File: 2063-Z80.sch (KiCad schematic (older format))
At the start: 80 parts, among them J1 Conn_01x05, J10 Conn_01x07, J11 Conn_02x03_Odd_Even, J2 DM3D-SF(41), J3 Conn_02x20_Counter_Clockwise, J4 Conn_02x05_Odd_Even, J5 Conn_02x05_Odd_Even, J6 0548190519, J7 Conn_02x13_Top_Bottom, J8 Conn_01x05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

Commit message: Clean up BOM values & formatting
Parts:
- J11: value Conn_02x03_Odd_Even -> Conn_02x03
- J3: value Conn_02x20_Counter_Clockwise -> Conn_02x20
- J4, J5: value Conn_02x05_Odd_Even -> Conn_02x05
- J7: value Conn_02x13_Top_Bottom -> Conn_02x13
- LOGO1, LOGO2: value Logo_Open_Hardware_Small -> OSHW_Logo
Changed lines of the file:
@@
 P 15550 5900
 F 0 "J3" H 15600 6950 50  0000 C CNN
-F 1 "Conn_02x20_Counter_Clockwise" H 15600 6926 50  0001 C CNN
+F 1 "Conn_02x20" H 15600 6926 50  0001 C CNN
 F 2 "jb-footprint:PinHeader_2x20_P2.54mm_Vertical_counterclock" H 15550 5900 50  0001 C CNN
 F 3 "https://drawings-pdf.s3.amazonaws.com/11636.pdf" H 15550 5900 50  0001 C CNN
@@
 P 15550 3650
 F 0 "J7" H 15600 4400 50  0000 C CNN
-F 1 "Conn_02x13_Top_Bottom" H 15600 4376 50  0001 C CNN
+F 1 "Conn_02x13" H 15600 4376 50  0001 C CNN
 F 2 "jb-footprint:PinHeader_2x13_P2.54mm_Top_Bottom" H 15550 3650 50  0001 C CNN
 F 3 "https://drawings-pdf.s3.amazonaws.com/11636.pdf" H 15550 3650 50  0001 C CNN
@@
 AR Path="/611D78B5" Ref="LOGO1"  Part="1"
 F 0 "LOGO1" H 16250 9875 50  0001 C CNN
-F 1 "Logo_Open_Hardware_Small" H 16250 9375 50  0001 C CNN
+F 1 "OSHW_Logo" H 16250 9375 50  0001 C CNN
 F 2 "Symbol:OSHW-Logo_11.4x12mm_SilkScreen" H 16250 9600 50  0001 C CNN
 F 3 "" H 16250 9600 50  0001 C CNN
@@
 AR Path="/61291DA5" Ref="LOGO2"  Part="1"
 F 0 "LOGO2" H 16200 8125 50  0001 C CNN
-F 1 "Logo_Open_Hardware_Small" H 16200 7625 50  0001 C CNN
+F 1 "OSHW_Logo" H 16200 7625 50  0001 C CNN
 F 2 "Symbol:OSHW-Logo_5.7x6mm_SilkScreen" H 16200 7850 50  0001 C CNN
 F 3 "" H 16200 7850 50  0001 C CNN
@@
 P 11600 8450
 F 0 "J4" H 11650 8775 50  0000 C CNN
-F 1 "Conn_02x05_Odd_Even" H 11650 8776 50  0001 C CNN
+F 1 "Conn_02x05" H 11650 8776 50  0001 C CNN
 F 2 "Connector_PinHeader_2.54mm:PinHeader_2x05_P2.54mm_Vertical" H 11600 8450 50  0001 C CNN
 F 3 "" H 11600 8450 50  0001 C CNN
@@
 P 11650 9650
 F 0 "J5" H 11700 9975 50  0000 C CNN
-F 1 "Conn_02x05_Odd_Even" H 11700 9976 50  0001 C CNN
+F 1 "Conn_02x05" H 11700 9976 50  0001 C CNN
 F 2 "Connector_PinHeader_2.54mm:PinHeader_2x05_P2.54mm_Vertical" H 11650 9650 50  0001 C CNN
 F 3 "" H 11650 9650 50  0001 C CNN
@@
 P 11800 3150
 F 0 "J11" H 11850 3350 50  0000 C CNN
-F 1 "Conn_02x03_Odd_Even" H 11850 3376 50  0001 C CNN
+F 1 "Conn_02x03" H 11850 3376 50  0001 C CNN
 F 2 "Connector_PinHeader_2.54mm:PinHeader_2x03_P2.54mm_Vertical" H 11800 3150 50  0001 C CNN
 F 3 "https://app.adam-tech.com/products/download/data_sheet/202065/ph2-xx-ua-data-sheet.pdf" H 11800 3150 50  0001 C CNN

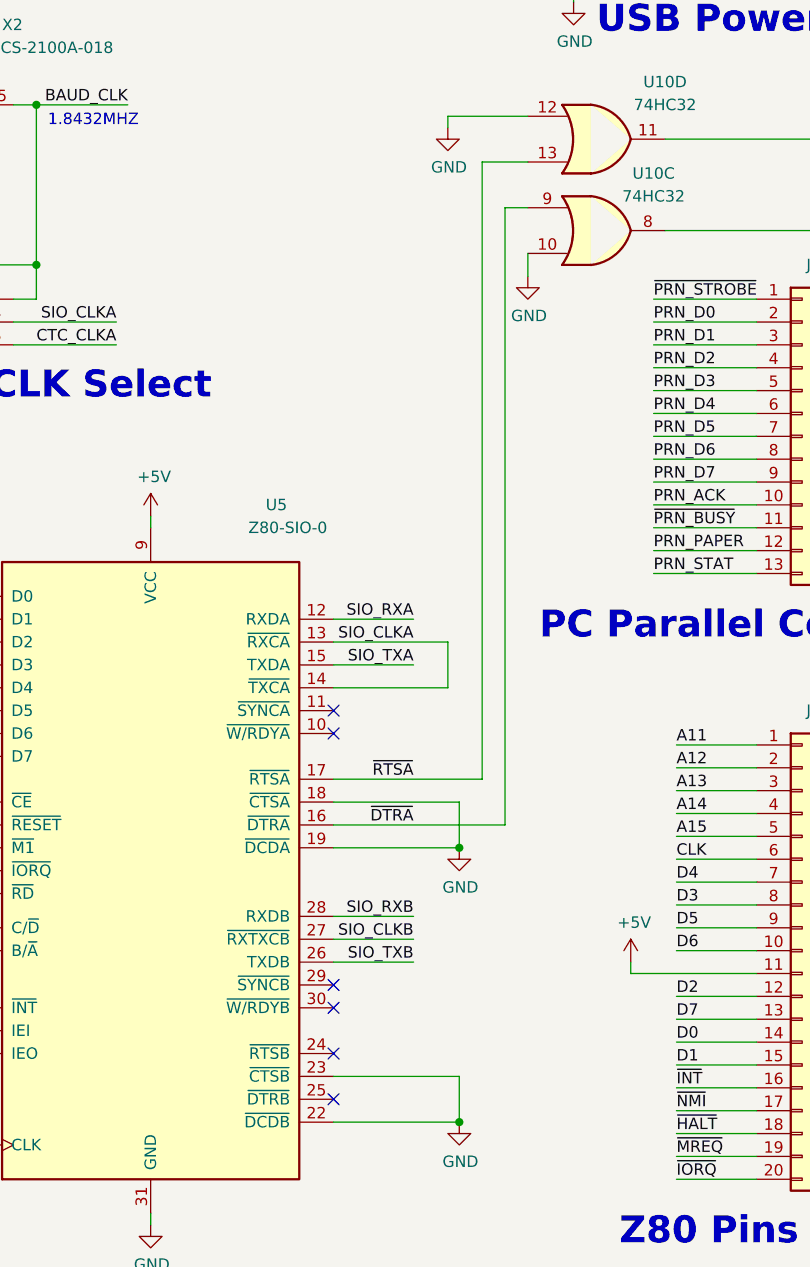
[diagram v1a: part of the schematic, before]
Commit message: Move ~PRN_LF from U5.17 to U5.25
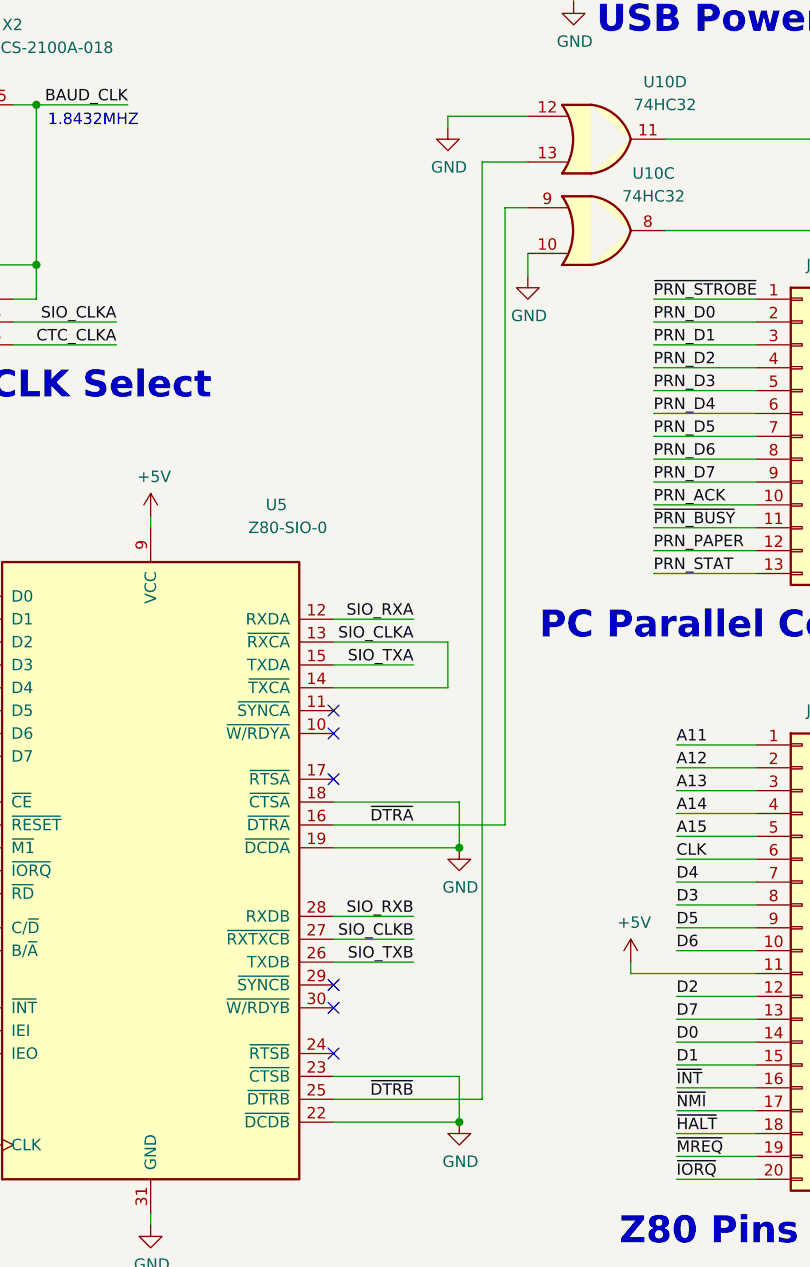
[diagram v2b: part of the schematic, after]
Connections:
- net ~DTRB: now reaches U5.25 (~DTRB)
- net ~DTRB: now also U10.13
- net ~RTSA: no longer names the net of U5.17 (~RTSA)
- net ~RTSA: no longer U10.13
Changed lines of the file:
@@
 Sheet 1 1
 Title "Z80 Retro Board"
-Date "2021-10-13"
-Rev "3"
+Date "2021-12-01"
+Rev "4"
 Comp ""
 Comment1 ""
@@
 	13500 6650 14050 6650
 NoConn ~ 13500 6350
-NoConn ~ 13500 6550
 Text Label 750  1600 0    50   ~ 0
 ~IORQ_70
@@
 Text Label 2750 4200 0    50   ~ 0
 BA15
-Text Label 13850 5150 2    50   ~ 0
-~RTSA
 Wire Wire Line
-	14150 2450 14150 5150
+	14150 2450 14150 6550
 $Comp
 L power:GND #PWR0156
@@
 Wire Wire Line
 	7250 700  7250 750
-Wire Wire Line
-	13500 5150 14150 5150
 Connection ~ 4900 1450
 Connection ~ 4900 1650
@@
 	1    0    0    -1
 $EndComp
+NoConn ~ 13500 5150
+Wire Wire Line
+	13500 6550 14150 6550
+Text Label 13850 6550 2    50   ~ 0
+~DTRB
 $EndSCHEMATC

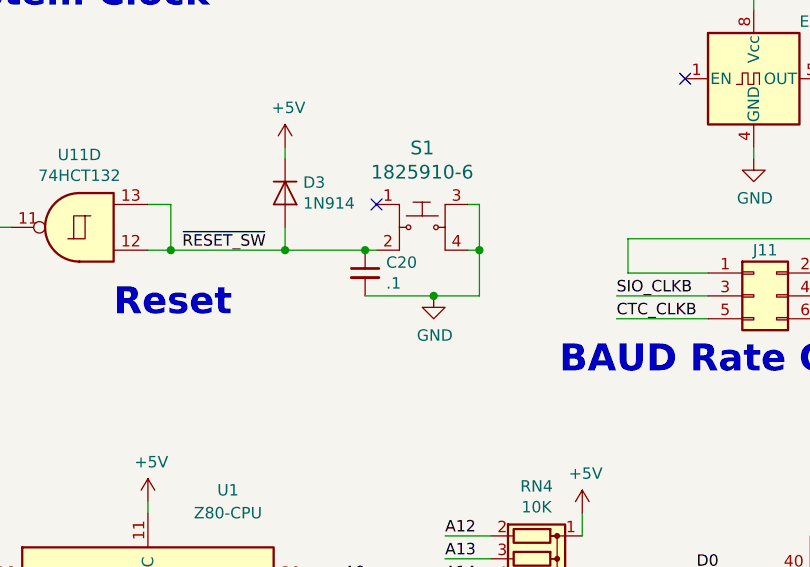
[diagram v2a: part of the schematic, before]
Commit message: Change C20 to .47uF to make RESET last 4X longer
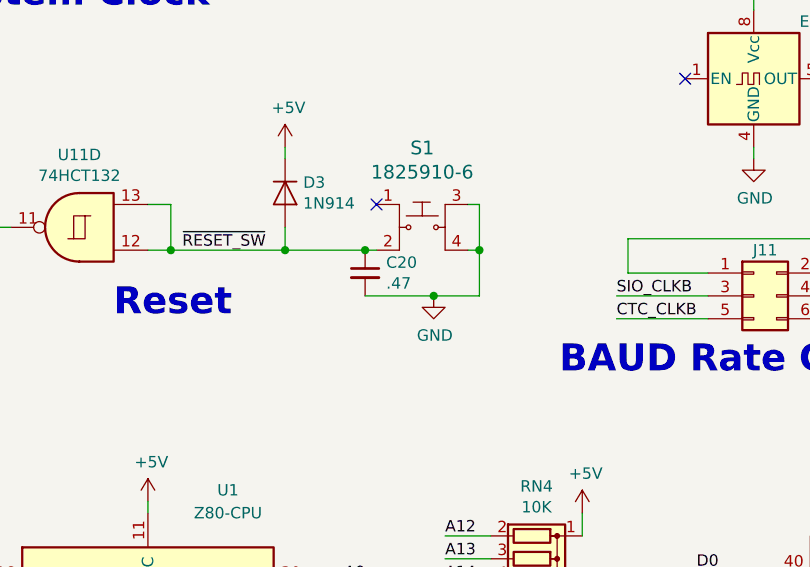
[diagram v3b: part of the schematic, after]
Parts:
- C1, C10, C11, C12, C13, C14, C15, C16, C2, C21, C22, C23, C3, C4, C5, C6, C7, C8, C9: Digi-Key_PN 399-9859-1-ND‎ -> 399-9859-1-ND
- C20: value .1 -> .47; Description CAP CER 0.1UF 50V Z5U RADIAL -> CAP CER 0.47UF 50V X7R RADIAL; Digi-Key_PN 399-9859-1-ND‎ -> 399-14039-1-ND; MPN ‎C315C104M5U5TA7303‎ -> C315C474K5R5TA7303
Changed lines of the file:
@@
 F 2 "Capacitor_THT:C_Disc_D3.0mm_W2.0mm_P2.50mm" H 4000 950 50  0001 C CNN
 F 3 "https://api.kemet.com/component-edge/download/specsheet/C315C104M5U5TA7303.pdf" H 4000 950 50  0001 C CNN
-F 4 "399-9859-1-ND‎" H 4000 950 50  0001 C CNN "Digi-Key_PN"
+F 4 "399-9859-1-ND" H 4000 950 50  0001 C CNN "Digi-Key_PN"
 F 5 "‎C315C104M5U5TA7303‎" H 4000 950 50  0001 C CNN "MPN"
 F 6 "CAP CER 0.1UF 50V Z5U RADIAL" H 4000 950 50  0001 C CNN "Description"
@@
 F 2 "Capacitor_THT:C_Disc_D3.0mm_W2.0mm_P2.50mm" H 4300 950 50  0001 C CNN
 F 3 "https://api.kemet.com/component-edge/download/specsheet/C315C104M5U5TA7303.pdf" H 4300 950 50  0001 C CNN
-F 4 "399-9859-1-ND‎" H 4300 950 50  0001 C CNN "Digi-Key_PN"
+F 4 "399-9859-1-ND" H 4300 950 50  0001 C CNN "Digi-Key_PN"
 F 5 "‎C315C104M5U5TA7303‎" H 4300 950 50  0001 C CNN "MPN"
 F 6 "CAP CER 0.1UF 50V Z5U RADIAL" H 4300 950 50  0001 C CNN "Description"
@@
 F 2 "Capacitor_THT:C_Disc_D3.0mm_W2.0mm_P2.50mm" H 4600 950 50  0001 C CNN
 F 3 "https://api.kemet.com/component-edge/download/specsheet/C315C104M5U5TA7303.pdf" H 4600 950 50  0001 C CNN
-F 4 "399-9859-1-ND‎" H 4600 950 50  0001 C CNN "Digi-Key_PN"
+F 4 "399-9859-1-ND" H 4600 950 50  0001 C CNN "Digi-Key_PN"
 F 5 "‎C315C104M5U5TA7303‎" H 4600 950 50  0001 C CNN "MPN"
 F 6 "CAP CER 0.1UF 50V Z5U RADIAL" H 4600 950 50  0001 C CNN "Description"
@@
 F 2 "Capacitor_THT:C_Disc_D3.0mm_W2.0mm_P2.50mm" H 4900 950 50  0001 C CNN
 F 3 "https://api.kemet.com/component-edge/download/specsheet/C315C104M5U5TA7303.pdf" H 4900 950 50  0001 C CNN
-F 4 "399-9859-1-ND‎" H 4900 950 50  0001 C CNN "Digi-Key_PN"
+F 4 "399-9859-1-ND" H 4900 950 50  0001 C CNN "Digi-Key_PN"
 F 5 "‎C315C104M5U5TA7303‎" H 4900 950 50  0001 C CNN "MPN"
 F 6 "CAP CER 0.1UF 50V Z5U RADIAL" H 4900 950 50  0001 C CNN "Description"
@@
 F 2 "Capacitor_THT:C_Disc_D3.0mm_W2.0mm_P2.50mm" H 5200 950 50  0001 C CNN
 F 3 "https://api.kemet.com/component-edge/download/specsheet/C315C104M5U5TA7303.pdf" H 5200 950 50  0001 C CNN
-F 4 "399-9859-1-ND‎" H 5200 950 50  0001 C CNN "Digi-Key_PN"
+F 4 "399-9859-1-ND" H 5200 950 50  0001 C CNN "Digi-Key_PN"
 F 5 "‎C315C104M5U5TA7303‎" H 5200 950 50  0001 C CNN "MPN"
 F 6 "CAP CER 0.1UF 50V Z5U RADIAL" H 5200 950 50  0001 C CNN "Description"
@@
 F 2 "Capacitor_THT:C_Disc_D3.0mm_W2.0mm_P2.50mm" H 7000 8400 50  0001 C CNN
 F 3 "https://api.kemet.com/component-edge/download/specsheet/C315C104M5U5TA7303.pdf" H 7000 8400 50  0001 C CNN
-F 4 "399-9859-1-ND‎" H 7000 8400 50  0001 C CNN "Digi-Key_PN"
+F 4 "399-9859-1-ND" H 7000 8400 50  0001 C CNN "Digi-Key_PN"
 F 5 "‎C315C104M5U5TA7303‎" H 7000 8400 50  0001 C CNN "MPN"
 F 6 "CAP CER 0.1UF 50V Z5U RADIAL" H 7000 8400 50  0001 C CNN "Description"
@@
 F 2 "Capacitor_THT:C_Disc_D3.0mm_W2.0mm_P2.50mm" H 9150 8350 50  0001 C CNN
 F 3 "https://api.kemet.com/component-edge/download/specsheet/C315C104M5U5TA7303.pdf" H 9150 8350 50  0001 C CNN
-F 4 "399-9859-1-ND‎" H 9150 8350 50  0001 C CNN "Digi-Key_PN"
+F 4 "399-9859-1-ND" H 9150 8350 50  0001 C CNN "Digi-Key_PN"
 F 5 "‎C315C104M5U5TA7303‎" H 9150 8350 50  0001 C CNN "MPN"
 F 6 "CAP CER 0.1UF 50V Z5U RADIAL" H 9150 8350 50  0001 C CNN "Description"
@@
 F 2 "Capacitor_THT:C_Disc_D3.0mm_W2.0mm_P2.50mm" H 9200 8750 50  0001 C CNN
 F 3 "https://api.kemet.com/component-edge/download/specsheet/C315C104M5U5TA7303.pdf" H 9200 8750 50  0001 C CNN
-F 4 "399-9859-1-ND‎" H 9200 8750 50  0001 C CNN "Digi-Key_PN"
+F 4 "399-9859-1-ND" H 9200 8750 50  0001 C CNN "Digi-Key_PN"
 F 5 "‎C315C104M5U5TA7303‎" H 9200 8750 50  0001 C CNN "MPN"
 F 6 "CAP CER 0.1UF 50V Z5U RADIAL" H 9200 8750 50  0001 C CNN "Description"
@@
 F 2 "Capacitor_THT:C_Disc_D3.0mm_W2.0mm_P2.50mm" H 9200 9050 50  0001 C CNN
 F 3 "https://api.kemet.com/component-edge/download/specsheet/C315C104M5U5TA7303.pdf" H 9200 9050 50  0001 C CNN
-F 4 "399-9859-1-ND‎" H 9200 9050 50  0001 C CNN "Digi-Key_PN"
+F 4 "399-9859-1-ND" H 9200 9050 50  0001 C CNN "Digi-Key_PN"
 F 5 "‎C315C104M5U5TA7303‎" H 9200 9050 50  0001 C CNN "MPN"
 F 6 "CAP CER 0.1UF 50V Z5U RADIAL" H 9200 9050 50  0001 C CNN "Description"
@@
 F 2 "Capacitor_THT:C_Disc_D3.0mm_W2.0mm_P2.50mm" H 5500 950 50  0001 C CNN
 F 3 "https://api.kemet.com/component-edge/download/specsheet/C315C104M5U5TA7303.pdf" H 5500 950 50  0001 C CNN
-F 4 "399-9859-1-ND‎" H 5500 950 50  0001 C CNN "Digi-Key_PN"
+F 4 "399-9859-1-ND" H 5500 950 50  0001 C CNN "Digi-Key_PN"
 F 5 "‎C315C104M5U5TA7303‎" H 5500 950 50  0001 C CNN "MPN"
 F 6 "CAP CER 0.1UF 50V Z5U RADIAL" H 5500 950 50  0001 C CNN "Description"
@@
 F 2 "Capacitor_THT:C_Disc_D3.0mm_W2.0mm_P2.50mm" H 5200 1550 50  0001 C CNN
 F 3 "https://api.kemet.com/component-edge/download/specsheet/C315C104M5U5TA7303.pdf" H 5200 1550 50  0001 C CNN
-F 4 "399-9859-1-ND‎" H 5200 1550 50  0001 C CNN "Digi-Key_PN"
+F 4 "399-9859-1-ND" H 5200 1550 50  0001 C CNN "Digi-Key_PN"
 F 5 "‎C315C104M5U5TA7303‎" H 5200 1550 50  0001 C CNN "MPN"
 F 6 "CAP CER 0.1UF 50V Z5U RADIAL" H 5200 1550 50  0001 C CNN "Description"
@@
 F 2 "Capacitor_THT:C_Disc_D3.0mm_W2.0mm_P2.50mm" H 5500 1550 50  0001 C CNN
 F 3 "https://api.kemet.com/component-edge/download/specsheet/C315C104M5U5TA7303.pdf" H 5500 1550 50  0001 C CNN
-F 4 "399-9859-1-ND‎" H 5500 1550 50  0001 C CNN "Digi-Key_PN"
+F 4 "399-9859-1-ND" H 5500 1550 50  0001 C CNN "Digi-Key_PN"
 F 5 "‎C315C104M5U5TA7303‎" H 5500 1550 50  0001 C CNN "MPN"
 F 6 "CAP CER 0.1UF 50V Z5U RADIAL" H 5500 1550 50  0001 C CNN "Description"
@@
 F 2 "Capacitor_THT:C_Disc_D3.0mm_W2.0mm_P2.50mm" H 3700 1550 50  0001 C CNN
 F 3 "https://api.kemet.com/component-edge/download/specsheet/C315C104M5U5TA7303.pdf" H 3700 1550 50  0001 C CNN
-F 4 "399-9859-1-ND‎" H 3700 1550 50  0001 C CNN "Digi-Key_PN"
+F 4 "399-9859-1-ND" H 3700 1550 50  0001 C CNN "Digi-Key_PN"
 F 5 "‎C315C104M5U5TA7303‎" H 3700 1550 50  0001 C CNN "MPN"
 F 6 "CAP CER 0.1UF 50V Z5U RADIAL" H 3700 1550 50  0001 C CNN "Description"
@@
 F 2 "Capacitor_THT:C_Disc_D3.0mm_W2.0mm_P2.50mm" H 4000 1550 50  0001 C CNN
 F 3 "https://api.kemet.com/component-edge/download/specsheet/C315C104M5U5TA7303.pdf" H 4000 1550 50  0001 C CNN
-F 4 "399-9859-1-ND‎" H 4000 1550 50  0001 C CNN "Digi-Key_PN"
+F 4 "399-9859-1-ND" H 4000 1550 50  0001 C CNN "Digi-Key_PN"
 F 5 "‎C315C104M5U5TA7303‎" H 4000 1550 50  0001 C CNN "MPN"
 F 6 "CAP CER 0.1UF 50V Z5U RADIAL" H 4000 1550 50  0001 C CNN "Description"
@@
 F 2 "Capacitor_THT:C_Disc_D3.0mm_W2.0mm_P2.50mm" H 4300 1550 50  0001 C CNN
 F 3 "https://api.kemet.com/component-edge/download/specsheet/C315C104M5U5TA7303.pdf" H 4300 1550 50  0001 C CNN
-F 4 "399-9859-1-ND‎" H 4300 1550 50  0001 C CNN "Digi-Key_PN"
+F 4 "399-9859-1-ND" H 4300 1550 50  0001 C CNN "Digi-Key_PN"
 F 5 "‎C315C104M5U5TA7303‎" H 4300 1550 50  0001 C CNN "MPN"
 F 6 "CAP CER 0.1UF 50V Z5U RADIAL" H 4300 1550 50  0001 C CNN "Description"
@@
 F 2 "Capacitor_THT:C_Disc_D3.0mm_W2.0mm_P2.50mm" H 4600 1550 50  0001 C CNN
 F 3 "https://api.kemet.com/component-edge/download/specsheet/C315C104M5U5TA7303.pdf" H 4600 1550 50  0001 C CNN
-F 4 "399-9859-1-ND‎" H 4600 1550 50  0001 C CNN "Digi-Key_PN"
+F 4 "399-9859-1-ND" H 4600 1550 50  0001 C CNN "Digi-Key_PN"
 F 5 "‎C315C104M5U5TA7303‎" H 4600 1550 50  0001 C CNN "MPN"
 F 6 "CAP CER 0.1UF 50V Z5U RADIAL" H 4600 1550 50  0001 C CNN "Description"
@@
 F 2 "Capacitor_THT:C_Disc_D3.0mm_W2.0mm_P2.50mm" H 4900 1550 50  0001 C CNN
 F 3 "https://api.kemet.com/component-edge/download/specsheet/C315C104M5U5TA7303.pdf" H 4900 1550 50  0001 C CNN
-F 4 "399-9859-1-ND‎" H 4900 1550 50  0001 C CNN "Digi-Key_PN"
+F 4 "399-9859-1-ND" H 4900 1550 50  0001 C CNN "Digi-Key_PN"
 F 5 "‎C315C104M5U5TA7303‎" H 4900 1550 50  0001 C CNN "MPN"
 F 6 "CAP CER 0.1UF 50V Z5U RADIAL" H 4900 1550 50  0001 C CNN "Description"
@@
 P 10100 3050
 F 0 "C20" H 10192 3096 50  0000 L CNN
-F 1 ".1" H 10192 3005 50  0000 L CNN
+F 1 ".47" H 10192 3005 50  0000 L CNN
 F 2 "Capacitor_THT:C_Disc_D3.0mm_W2.0mm_P2.50mm" H 10100 3050 50  0001 C CNN
-F 3 "https://api.kemet.com/component-edge/download/specsheet/C315C104M5U5TA7303.pdf" H 10100 3050 50  0001 C CNN
-F 4 "399-9859-1-ND‎" H 10100 3050 50  0001 C CNN "Digi-Key_PN"
-F 5 "‎C315C104M5U5TA7303‎" H 10100 3050 50  0001 C CNN "MPN"
-F 6 "CAP CER 0.1UF 50V Z5U RADIAL" H 10100 3050 50  0001 C CNN "Description"
+F 3 "https://api.kemet.com/component-edge/download/datasheet/C315C474K5R5TA7303.pdf" H 10100 3050 50  0001 C CNN
+F 4 "399-14039-1-ND" H 10100 3050 50  0001 C CNN "Digi-Key_PN"
+F 5 "C315C474K5R5TA7303" H 10100 3050 50  0001 C CNN "MPN"
+F 6 "CAP CER 0.47UF 50V X7R RADIAL" H 10100 3050 50  0001 C CNN "Description"
 F 7 "KEMET" H 10100 3050 50  0001 C CNN "Manufacturer"
 	1    10100 3050
@@
 F 2 "Capacitor_THT:C_Disc_D3.0mm_W2.0mm_P2.50mm" H 3700 950 50  0001 C CNN
 F 3 "https://api.kemet.com/component-edge/download/specsheet/C315C104M5U5TA7303.pdf" H 3700 950 50  0001 C CNN
-F 4 "399-9859-1-ND‎" H 3700 950 50  0001 C CNN "Digi-Key_PN"
+F 4 "399-9859-1-ND" H 3700 950 50  0001 C CNN "Digi-Key_PN"
 F 5 "‎C315C104M5U5TA7303‎" H 3700 950 50  0001 C CNN "MPN"
 F 6 "CAP CER 0.1UF 50V Z5U RADIAL" H 3700 950 50  0001 C CNN "Description"
@@
 F 2 "Capacitor_THT:C_Disc_D3.0mm_W2.0mm_P2.50mm" H 5850 950 50  0001 C CNN
 F 3 "https://api.kemet.com/component-edge/download/specsheet/C315C104M5U5TA7303.pdf" H 5850 950 50  0001 C CNN
-F 4 "399-9859-1-ND‎" H 5850 950 50  0001 C CNN "Digi-Key_PN"
+F 4 "399-9859-1-ND" H 5850 950 50  0001 C CNN "Digi-Key_PN"
 F 5 "‎C315C104M5U5TA7303‎" H 5850 950 50  0001 C CNN "MPN"
 F 6 "CAP CER 0.1UF 50V Z5U RADIAL" H 5850 950 50  0001 C CNN "Description"

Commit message: Add alternate source for SD socket.
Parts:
- J2: Digi-Key_PN H126097CT-ND‎ -> H126097CT-ND (alternate: 114-00841-68-1-ND)
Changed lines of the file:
@@
 F 2 "Connector_Card:microSD_HC_Hirose_DM3D-SF" H 16900 8900 50  0001 C CNN
 F 3 "https://www.hirose.com/product/document?clcode=CL0609-0033-6-00&productname=DM3AT-SF-PEJ2M5&series=DM3&documenttype=Catalog&lang=en&documentid=D49662_en" H 14850 8300 50  0001 C CNN
-F 4 "H126097CT-ND‎" H 14850 8200 50  0001 C CNN "Digi-Key_PN"
+F 4 "H126097CT-ND (alternate: 114-00841-68-1-ND)" H 14850 8200 50  0001 C CNN "Digi-Key_PN"
 F 5 "‎DM3D-SF(41)‎ " H 14850 8200 50  0001 C CNN "MPN"
 F 6 "CONN MICRO SD R/A PUSH-PULL SMD" H 14850 8200 50  0001 C CNN "Description"
